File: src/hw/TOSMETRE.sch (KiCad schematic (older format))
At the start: 51 parts, among them J2 Conn_Coaxial, J3 Conn_01x08_Male, J4 Barrel_Jack_Switch, J5 Conn_Coaxial, J6 Alim Piles, SW3 SW_DIP_x01, U1 18F1320, U3 LT1818, U5 LTC2305, U6 LT1818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

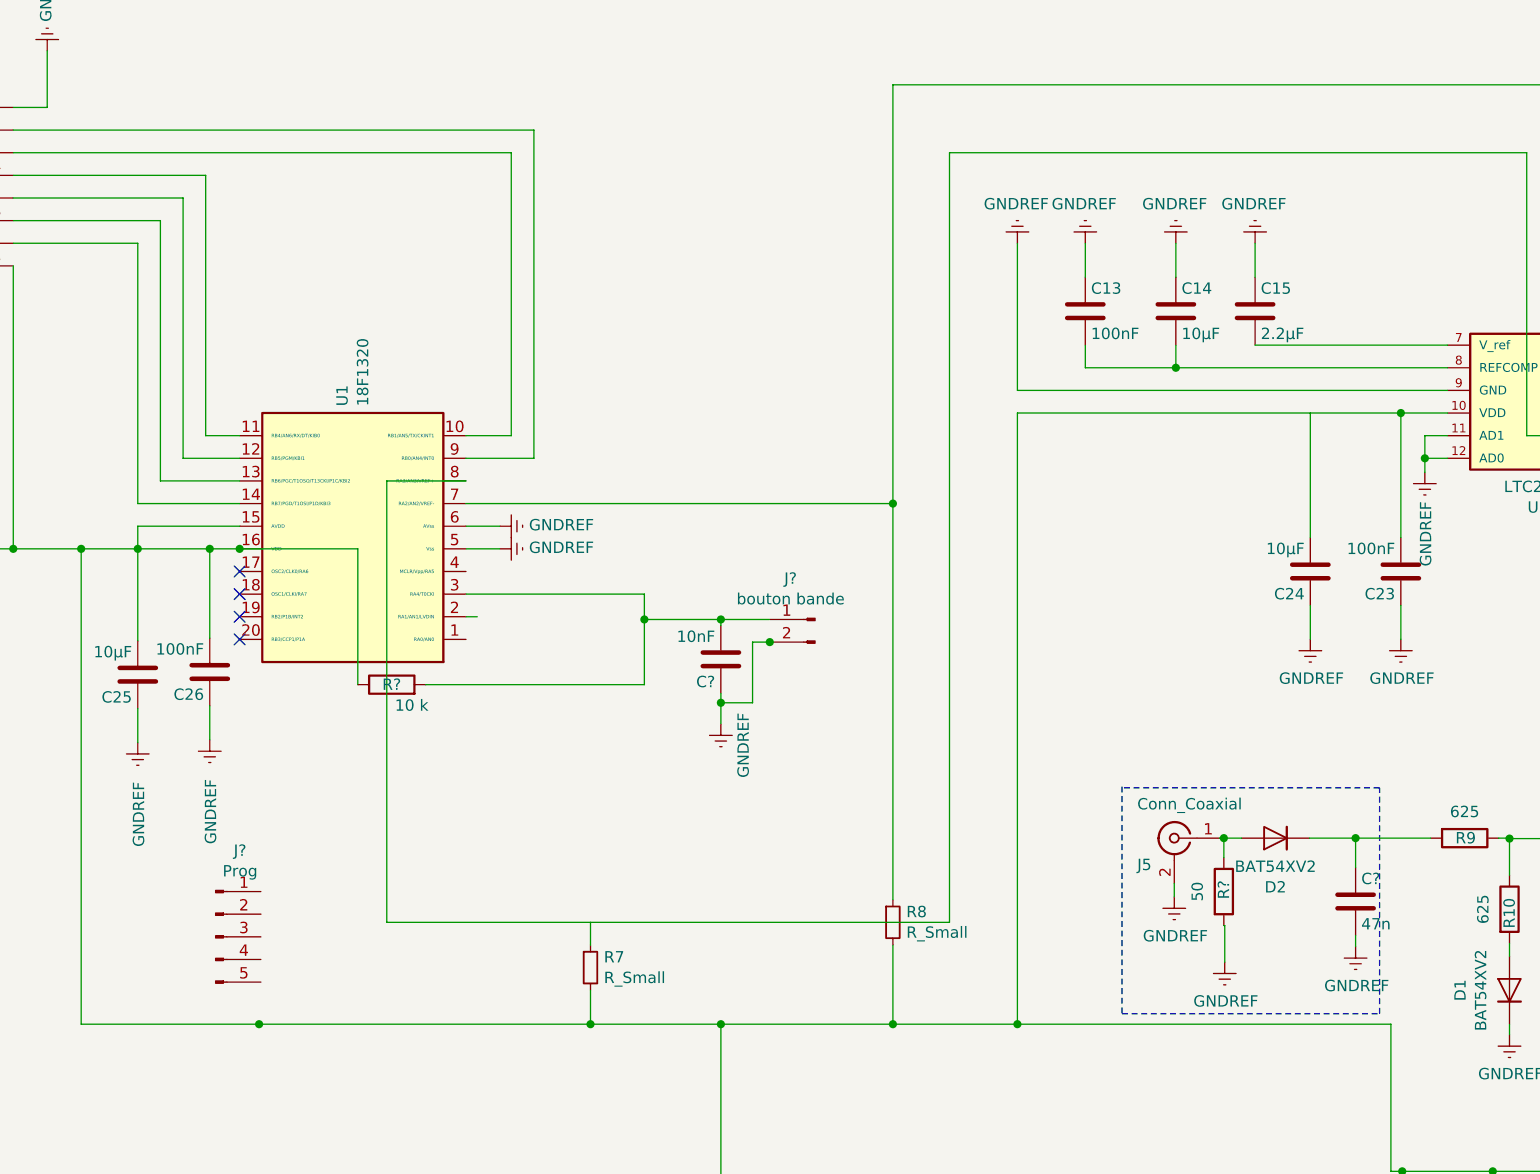
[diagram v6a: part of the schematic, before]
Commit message: #306 connecteur de prog
il faudra faire un pont sur le circuit imprime
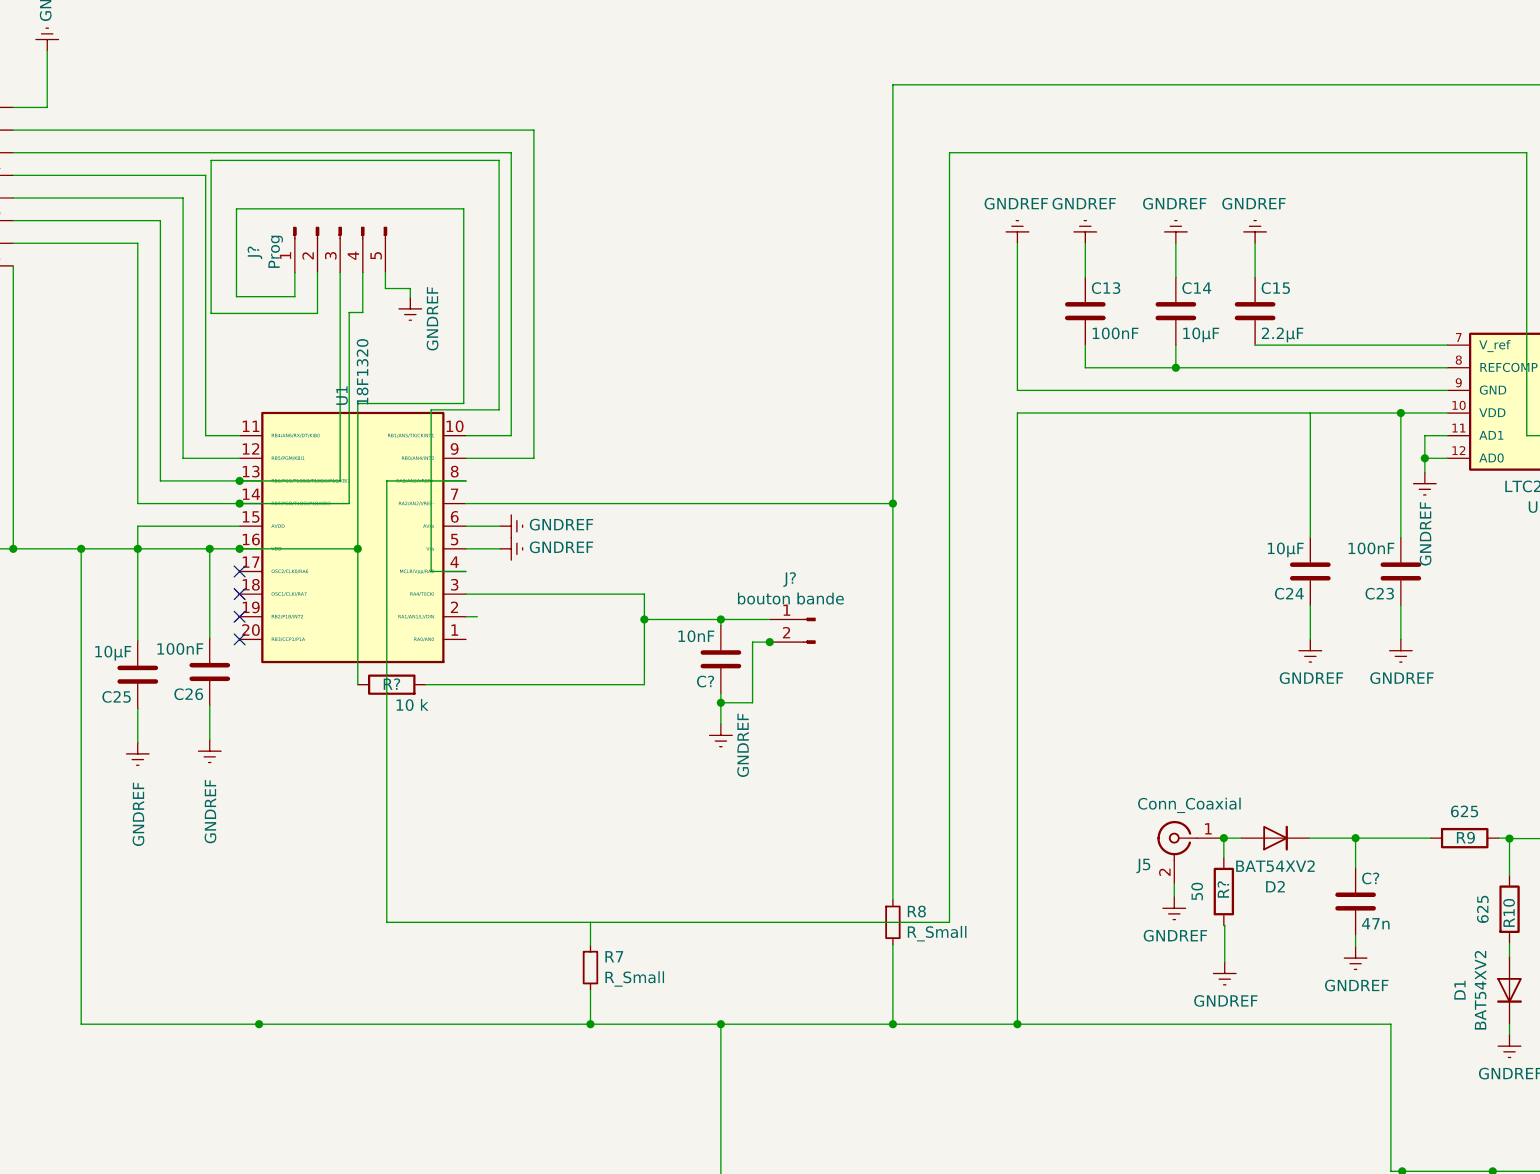
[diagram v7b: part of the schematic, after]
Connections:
- wire segments 217 -> 241
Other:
- moved on the sheet: J?
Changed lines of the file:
@@
 	8544 7678 8876 7678
-Wire Notes Line
-	7512 7450 7512 8454
-Wire Notes Line
-	7512 8454 8650 8454
-Wire Notes Line
-	8650 8454 8650 7456
-Wire Notes Line
-	8650 7456 7512 7456
 Wire Notes Line
 	6408 2034 7080 2034
@@
 Wire Wire Line
 	4264 6100 4614 6100
-$Comp
-L Device:R_Small R7
-U 1 1 5F3A7C96
-P 5164 8250
-F 0 "R7" H 5223 8296 50  0000 L CNN
-F 1 "R_Small" H 5223 8205 50  0000 L CNN
-F 2 "Resistor_SMD:R_1206_3216Metric" H 5164 8250 50  0001 C CNN
-F 3 "~" H 5164 8250 50  0001 C CNN
-	1    5164 8250
-	1    0    0    -1
-$EndComp
 Connection ~ 2914 6400
 Wire Wire Line
@@
 	3364 6000 3364 4850
 Wire Wire Line
-	3614 6100 3264 6100
-Wire Wire Line
 	3264 6100 3264 4950
-Wire Wire Line
-	3164 6200 3614 6200
 Wire Wire Line
 	4614 6000 4914 6000
@@
 L Connector:Conn_01x05_Male J?
 U 1 1 605F711F
-P 3508 8114
-F 0 "J?" H 3616 8495 50  0000 C CNN
-F 1 "Prog" H 3616 8404 50  0000 C CNN
-F 2 "" H 3508 8114 50  0001 C CNN
-F 3 "~" H 3508 8114 50  0001 C CNN
-	1    3508 8114
-	1    0    0    -1
+P 4058 4980
+F 0 "J?" H 4166 5361 50  0000 C CNN
+F 1 "Prog" H 4166 5270 50  0000 C CNN
+F 2 "" H 4058 4980 50  0001 C CNN
+F 3 "~" H 4058 4980 50  0001 C CNN
+	1    4058 4980
+	0    -1   1    0
 $EndComp
 Wire Wire Line
@@
 Wire Wire Line
 	5402 6712 5402 7000
+$Comp
+L power:GNDREF #PWR?
+U 1 1 60764C79
+P 4368 5290
+F 0 "#PWR?" H 4368 5040 50  0001 C CNN
+F 1 "GNDREF" V 4468 5340 50  0000 R CNN
+F 2 "" H 4368 5290 50  0001 C CNN
+F 3 "" H 4368 5290 50  0001 C CNN
+	1    4368 5290
+	1    0    0    -1
+$EndComp
+Wire Wire Line
+	4136 6400 4136 5758
+Wire Wire Line
+	4136 5758 4604 5758
+Wire Wire Line
+	4604 5758 4604 4898
+Wire Wire Line
+	4604 4898 3600 4898
+Wire Wire Line
+	3600 4898 3600 5286
+Wire Wire Line
+	3600 5286 3858 5286
+Wire Wire Line
+	3858 5286 3858 5180
+Connection ~ 4136 6400
+Wire Wire Line
+	4258 5180 4258 5250
+Wire Wire Line
+	4258 5250 4368 5250
+Wire Wire Line
+	4368 5250 4368 5290
+$Comp
+L Device:R_Small R7
+U 1 1 5F3A7C96
+P 5164 8250
+F 0 "R7" H 5223 8296 50  0000 L CNN
+F 1 "R_Small" H 5223 8205 50  0000 L CNN
+F 2 "Resistor_SMD:R_1206_3216Metric" H 5164 8250 50  0001 C CNN
+F 3 "~" H 5164 8250 50  0001 C CNN
+	1    5164 8250
+	1    0    0    -1
+$EndComp
+Wire Wire Line
+	4614 6500 4460 6500
+Wire Wire Line
+	4460 6500 4460 5786
+Wire Wire Line
+	4460 5786 4760 5786
+Wire Wire Line
+	4760 5786 4760 4684
+Wire Wire Line
+	4760 4684 3488 4684
+Wire Wire Line
+	3488 4684 3488 5360
+Wire Wire Line
+	3488 5360 3958 5360
+Wire Wire Line
+	3958 5360 3958 5180
+Wire Wire Line
+	4058 6100 4058 5180
+Wire Wire Line
+	3264 6100 3614 6100
+Connection ~ 3614 6100
+Wire Wire Line
+	3614 6100 4058 6100
+Wire Wire Line
+	4098 6200 4098 5356
+Wire Wire Line
+	4098 5356 4158 5356
+Wire Wire Line
+	4158 5356 4158 5180
+Wire Wire Line
+	3164 6200 3614 6200
+Connection ~ 3614 6200
+Wire Wire Line
+	3614 6200 4098 6200
 $EndSCHEMATC

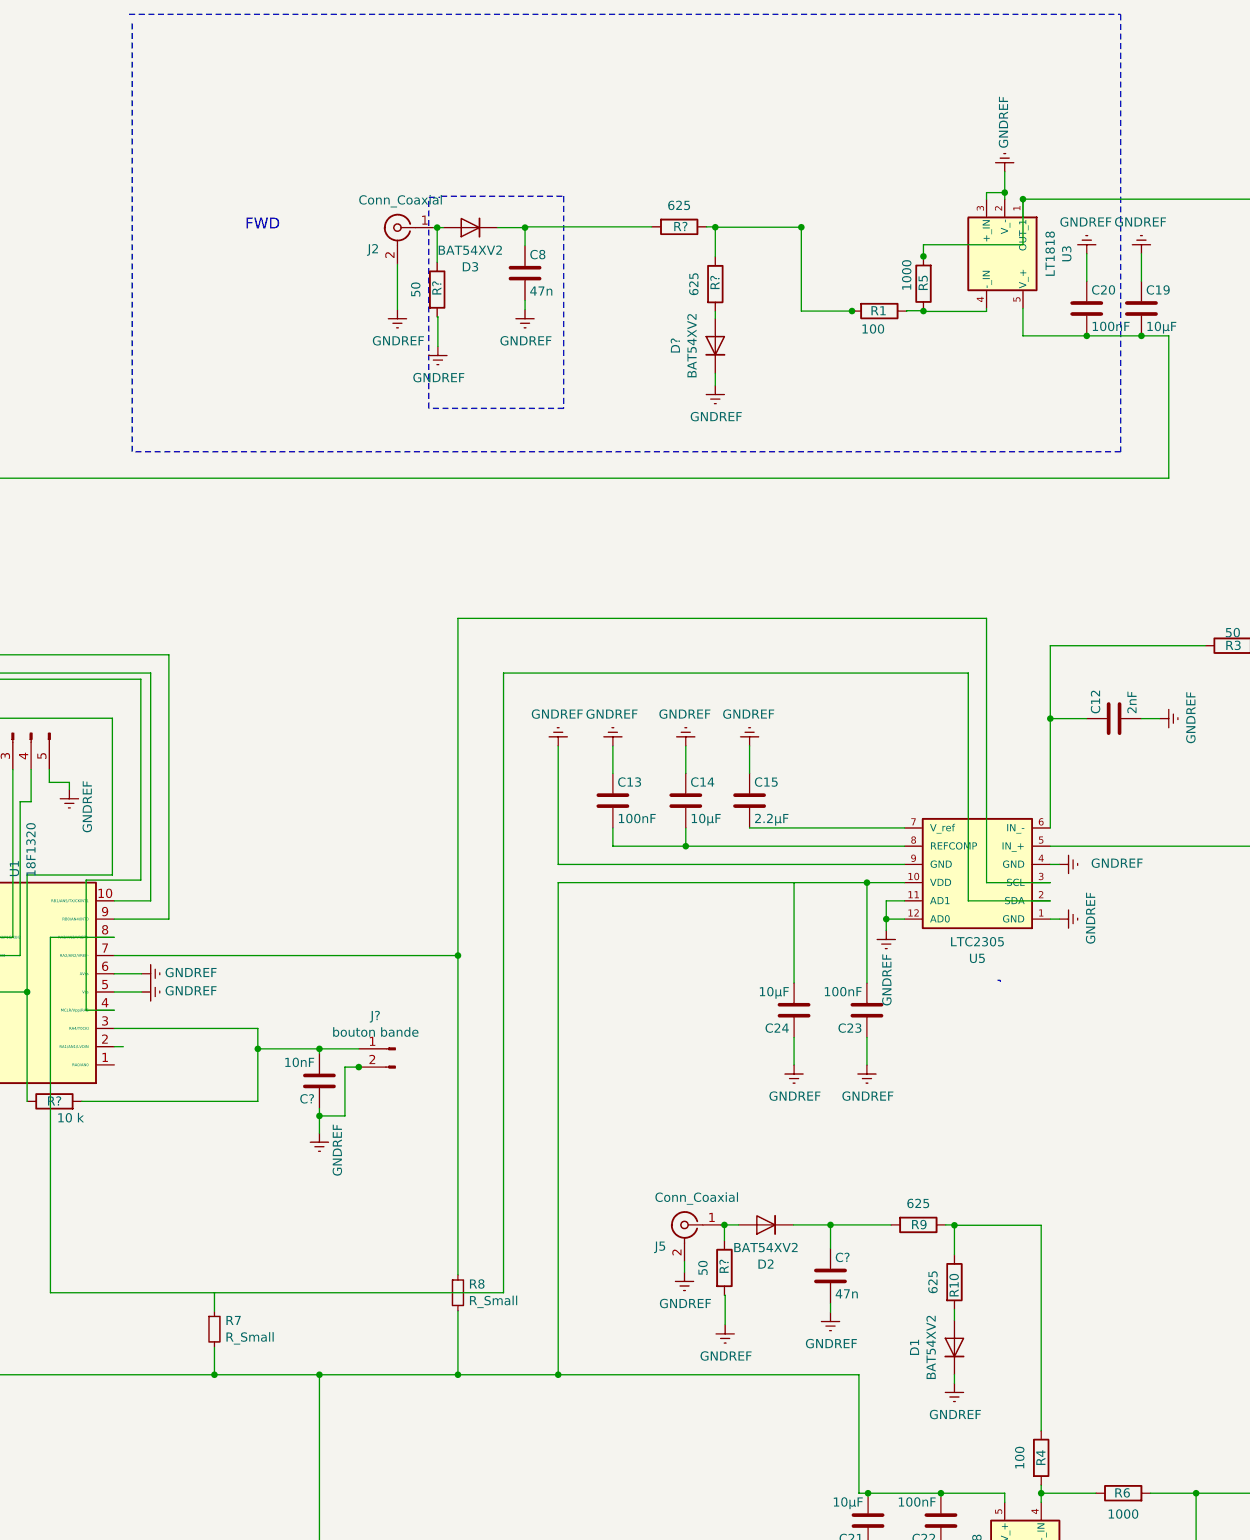
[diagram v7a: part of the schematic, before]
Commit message: #333 #302 #327
modif pont divisieur aop
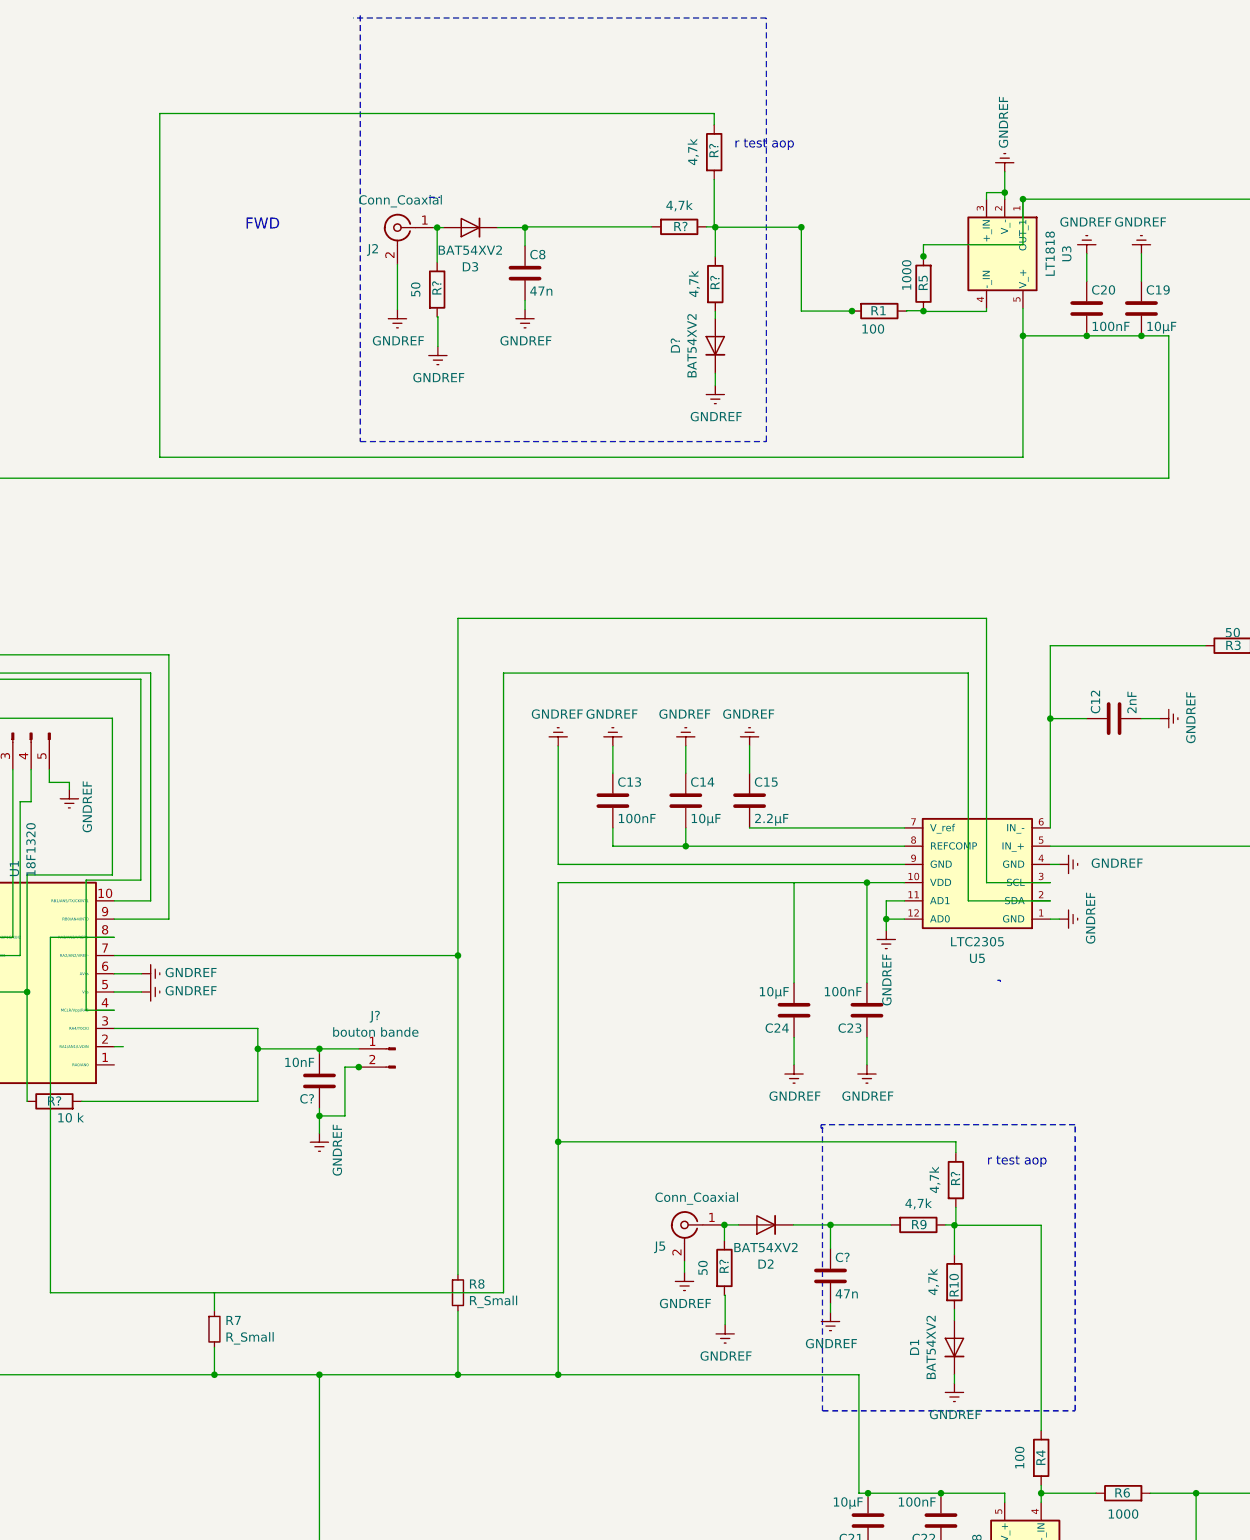
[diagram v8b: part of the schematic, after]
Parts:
- added R? (x2): 4,7k, Resistor_SMD:R_1206_3216Metric, symbol Device:R
- R10, R9, R? (x2): value 625 -> 4,7k
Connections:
- wire segments 241 -> 251
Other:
- note added: "r test aop"
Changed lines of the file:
@@
 	6500 8500 7050 8500
 Wire Wire Line
-	7050 5800 7050 8500
+	7050 5800 7050 7222
 Wire Wire Line
 	9750 5600 13600 5600
@@
 Connection ~ 9224 7680
 Wire Wire Line
-	9224 7680 9700 7680
-Wire Wire Line
 	9224 7678 9224 7680
 $Comp
@@
 P 9224 7992
 F 0 "R10" V 9224 8042 50  0000 R CNN
-F 1 "625" V 9108 7992 50  0000 C CNN
+F 1 "4,7k" V 9108 7992 50  0000 C CNN
 F 2 "Resistor_SMD:R_1206_3216Metric" V 9154 7992 50  0001 C CNN
 F 3 "~" H 9224 7992 50  0001 C CNN
@@
 P 9026 7678
 F 0 "R9" V 9026 7728 50  0000 R CNN
-F 1 "625" V 8910 7678 50  0000 C CNN
+F 1 "4,7k" V 8910 7678 50  0000 C CNN
 F 2 "Resistor_SMD:R_1206_3216Metric" V 8956 7678 50  0001 C CNN
 F 3 "~" H 9026 7678 50  0001 C CNN
@@
 P 7912 2516
 F 0 "R?" V 7912 2566 50  0000 R CNN
-F 1 "625" V 7796 2516 50  0000 C CNN
+F 1 "4,7k" V 7796 2516 50  0000 C CNN
 F 2 "Resistor_SMD:R_1206_3216Metric" V 7842 2516 50  0001 C CNN
 F 3 "~" H 7912 2516 50  0001 C CNN
@@
 P 7714 2202
 F 0 "R?" V 7714 2252 50  0000 R CNN
-F 1 "625" V 7598 2202 50  0000 C CNN
+F 1 "4,7k" V 7598 2202 50  0000 C CNN
 F 2 "Resistor_SMD:R_1206_3216Metric" V 7644 2202 50  0001 C CNN
 F 3 "~" H 7714 2202 50  0001 C CNN
@@
 	0    1    1    0
 $EndComp
-Wire Wire Line
-	7864 2202 7912 2202
 Wire Wire Line
 	10400 2800 10400 3581
@@
 Wire Wire Line
 	7912 3004 7912 3072
-Wire Notes Line
-	4696 1036 10136 1036
-Wire Notes Line
-	10136 1036 10136 3436
-Wire Notes Line
-	10136 3436 4712 3436
-Wire Notes Line
-	4712 3436 4712 1076
 Wire Wire Line
 	6868 2202 6868 2206
@@
 Wire Wire Line
 	8544 7678 8876 7678
-Wire Notes Line
-	6408 2034 7080 2034
-Wire Notes Line
-	7080 2034 7080 3198
-Wire Notes Line
-	7080 3198 6340 3198
-Wire Notes Line
-	6340 3198 6340 2040
 Wire Notes Line
 	6340 2040 6402 2040
@@
 Wire Wire Line
 	3614 6200 4098 6200
+$Comp
+L Device:R R?
+U 1 1 6049BB8F
+P 7906 1792
+F 0 "R?" V 7906 1842 50  0000 R CNN
+F 1 "4,7k" V 7790 1792 50  0000 C CNN
+F 2 "Resistor_SMD:R_1206_3216Metric" V 7836 1792 50  0001 C CNN
+F 3 "~" H 7906 1792 50  0001 C CNN
+	1    7906 1792
+	1    0    0    -1
+$EndComp
+Wire Wire Line
+	7906 1942 7906 2202
+Wire Wire Line
+	7864 2202 7916 2202
+Wire Wire Line
+	7906 1642 7906 1580
+Wire Wire Line
+	7906 1580 4864 1580
+Wire Wire Line
+	4864 1580 4864 3466
+Wire Wire Line
+	4864 3466 9600 3466
+Wire Wire Line
+	9600 3466 9600 2800
+Connection ~ 9600 2800
+$Comp
+L Device:R R?
+U 1 1 604D5A68
+P 9232 7432
+F 0 "R?" V 9232 7482 50  0000 R CNN
+F 1 "4,7k" V 9116 7432 50  0000 C CNN
+F 2 "Resistor_SMD:R_1206_3216Metric" V 9162 7432 50  0001 C CNN
+F 3 "~" H 9232 7432 50  0001 C CNN
+	1    9232 7432
+	1    0    0    -1
+$EndComp
+Wire Wire Line
+	9232 7582 9232 7680
+Wire Wire Line
+	9224 7680 9700 7680
+Wire Wire Line
+	9232 7282 9232 7222
+Wire Wire Line
+	9232 7222 7050 7222
+Connection ~ 7050 7222
+Wire Wire Line
+	7050 7222 7050 8500
+Text Notes 9402 7362 0    50   ~ 0
+r test aop
+Text Notes 8016 1782 0    50   ~ 0
+r test aop
+Wire Notes Line
+	5964 1042 5964 3380
+Wire Notes Line
+	5964 3380 8192 3380
+Wire Notes Line
+	8192 3380 8192 1056
+Wire Notes Line
+	8192 1056 5924 1056
+Wire Notes Line
+	8500 7140 8500 8698
+Wire Notes Line
+	8500 8698 9886 8698
+Wire Notes Line
+	9886 8698 9886 7128
+Wire Notes Line
+	9886 7128 8492 7128
+Wire Notes Line
+	8492 7128 8492 7148
+Wire Notes Line
+	8492 7148 8504 7148
 $EndSCHEMATC
